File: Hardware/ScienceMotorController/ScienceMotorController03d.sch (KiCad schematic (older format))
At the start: 16 parts

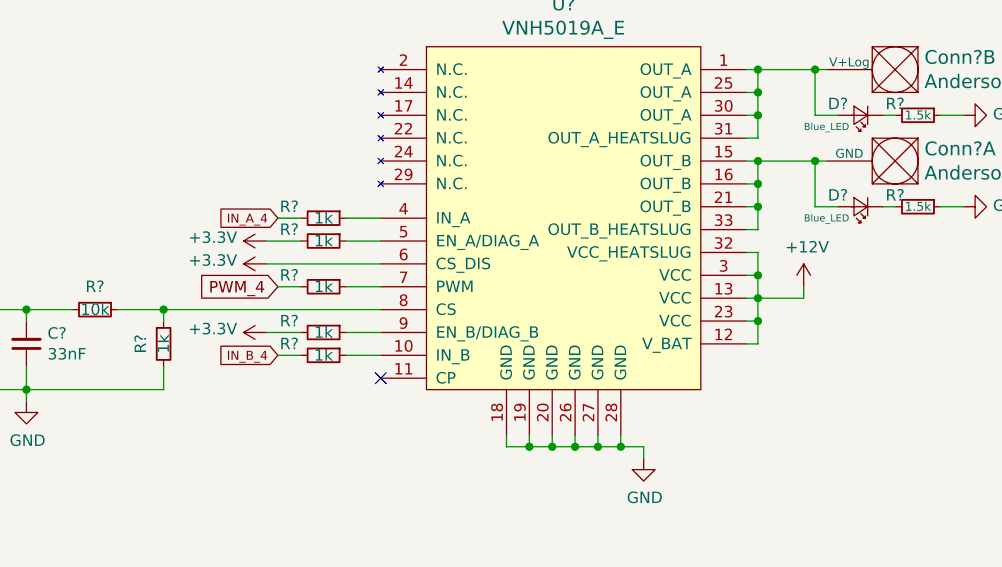
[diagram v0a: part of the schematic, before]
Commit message: changed everything to actuation, added schottky diode, added A/B flags to tiva
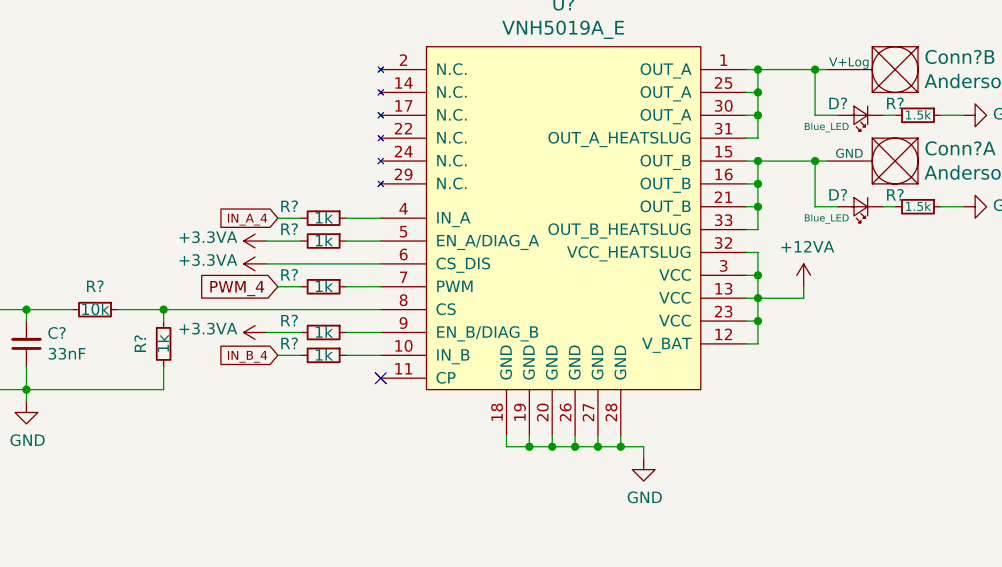
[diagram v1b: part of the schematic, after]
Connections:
- net +12V renamed +12VA
- net +3V3 renamed +3.3VA
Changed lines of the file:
@@
 	6800 4300 6800 4200
 Connection ~ 6800 4200
-$Comp
-L power:+12V #PWR?
-U 1 1 5FA97817
-P 7000 4050
-AR Path="/5F7D111E/5FA97817" Ref="#PWR?"  Part="1"
-AR Path="/5F7D111E/5FA6640B/5FA97817" Ref="#PWR?"  Part="1"
-F 0 "#PWR?" H 7000 3900 50  0001 C CNN
-F 1 "+12V" H 7015 4223 50  0000 C CNN
-F 2 "" H 7000 4050 50  0001 C CNN
-F 3 "" H 7000 4050 50  0001 C CNN
-	1    7000 4050
-	1    0    0    -1
-$EndComp
 Wire Wire Line
 	7000 4050 7000 4100
@@
 Wire Wire Line
 	4800 4250 4650 4250
-$Comp
-L power:+3.3V #PWR?
-U 1 1 5FA97858
-P 4650 4250
-AR Path="/5F7D111E/5FA97858" Ref="#PWR?"  Part="1"
-AR Path="/5F7D111E/5FA6640B/5FA97858" Ref="#PWR?"  Part="1"
-F 0 "#PWR?" H 4650 4100 50  0001 C CNN
-F 1 "+3.3V" V 4665 4378 50  0000 L CNN
-F 2 "" H 4650 4250 50  0001 C CNN
-F 3 "" H 4650 4250 50  0001 C CNN
-	1    4650 4250
-	0    -1   -1   0
-$EndComp
-$Comp
-L power:+3.3V #PWR?
-U 1 1 5FA9785E
-P 4650 3950
-AR Path="/5F7D111E/5FA9785E" Ref="#PWR?"  Part="1"
-AR Path="/5F7D111E/5FA6640B/5FA9785E" Ref="#PWR?"  Part="1"
-F 0 "#PWR?" H 4650 3800 50  0001 C CNN
-F 1 "+3.3V" V 4665 4078 50  0000 L CNN
-F 2 "" H 4650 3950 50  0001 C CNN
-F 3 "" H 4650 3950 50  0001 C CNN
-	1    4650 3950
-	0    -1   -1   0
-$EndComp
 Wire Wire Line
 	5150 3950 4650 3950
@@
 Wire Wire Line
 	5150 3850 5000 3850
-$Comp
-L power:+3.3V #PWR?
-U 1 1 5FA9786C
-P 4650 3850
-AR Path="/5F7D111E/5FA9786C" Ref="#PWR?"  Part="1"
-AR Path="/5F7D111E/5FA6640B/5FA9786C" Ref="#PWR?"  Part="1"
-F 0 "#PWR?" H 4650 3700 50  0001 C CNN
-F 1 "+3.3V" V 4665 3978 50  0000 L CNN
-F 2 "" H 4650 3850 50  0001 C CNN
-F 3 "" H 4650 3850 50  0001 C CNN
-	1    4650 3850
-	0    -1   -1   0
-$EndComp
 Wire Wire Line
 	4800 3850 4650 3850
@@
 Text Notes 7150 6900 0    197  ~ 0
 Sheet 03d: Motor Driver 4
+$Comp
+L power:+12VA #PWR?
+U 1 1 5F837D8D
+P 7000 4050
+F 0 "#PWR?" H 7000 3900 50  0001 C CNN
+F 1 "+12VA" H 7015 4223 50  0000 C CNN
+F 2 "" H 7000 4050 50  0001 C CNN
+F 3 "" H 7000 4050 50  0001 C CNN
+	1    7000 4050
+	1    0    0    -1
+$EndComp
+$Comp
+L power:+3.3VA #PWR?
+U 1 1 5F838A13
+P 4650 3850
+F 0 "#PWR?" H 4650 3700 50  0001 C CNN
+F 1 "+3.3VA" V 4665 3977 50  0000 L CNN
+F 2 "" H 4650 3850 50  0001 C CNN
+F 3 "" H 4650 3850 50  0001 C CNN
+	1    4650 3850
+	0    -1   -1   0
+$EndComp
+$Comp
+L power:+3.3VA #PWR?
+U 1 1 5F83A598
+P 4650 3950
+F 0 "#PWR?" H 4650 3800 50  0001 C CNN
+F 1 "+3.3VA" V 4665 4077 50  0000 L CNN
+F 2 "" H 4650 3950 50  0001 C CNN
+F 3 "" H 4650 3950 50  0001 C CNN
+	1    4650 3950
+	0    -1   -1   0
+$EndComp
+$Comp
+L power:+3.3VA #PWR?
+U 1 1 5F83A969
+P 4650 4250
+F 0 "#PWR?" H 4650 4100 50  0001 C CNN
+F 1 "+3.3VA" V 4665 4377 50  0000 L CNN
+F 2 "" H 4650 4250 50  0001 C CNN
+F 3 "" H 4650 4250 50  0001 C CNN
+	1    4650 4250
+	0    -1   -1   0
+$EndComp
 $EndSCHEMATC

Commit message: fixed hierarchical
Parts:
- added FB? (x2): Ferrite_Bead, symbol Device:Ferrite_Bead_Small
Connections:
- net at U?.1 (OUT_A), U?.25 (OUT_A), U?.30 (OUT_A)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: now also FB?.2; no longer Conn?.2 (V+Log), D?.2 (A)
- net at U?.15 (OUT_B), U?.16 (OUT_B), U?.21 (OUT_B)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: now also FB?.2; no longer Conn?.1 (GND), D?.2 (A)
- net IN_A_4 renamed In_A_4
- net IN_B_4 renamed In_B_4
- new net: Conn?.2 (V+Log), D?.2 (A), FB?.1
- new net: Conn?.1 (GND), D?.2 (A), FB?.1
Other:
- moved on the sheet: Conn?A, Conn?B, D?, R?

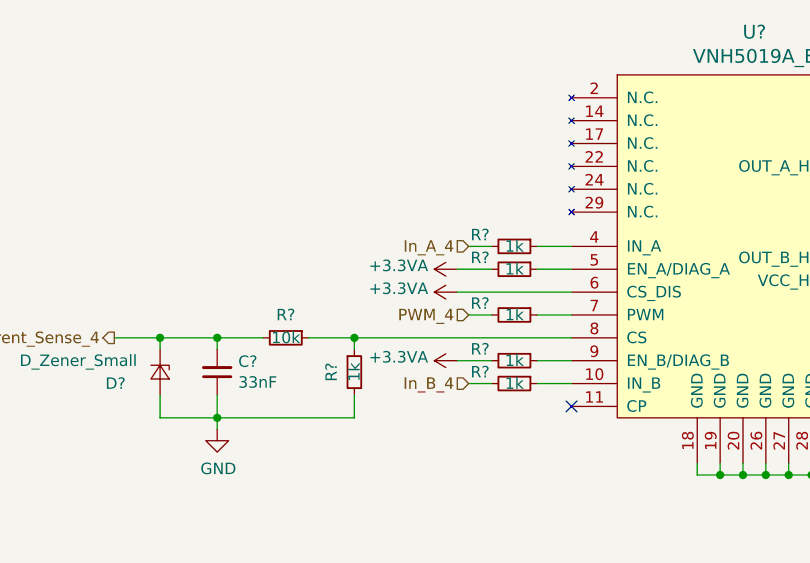
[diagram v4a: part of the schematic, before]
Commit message: Fixed 3.3V, added encoders
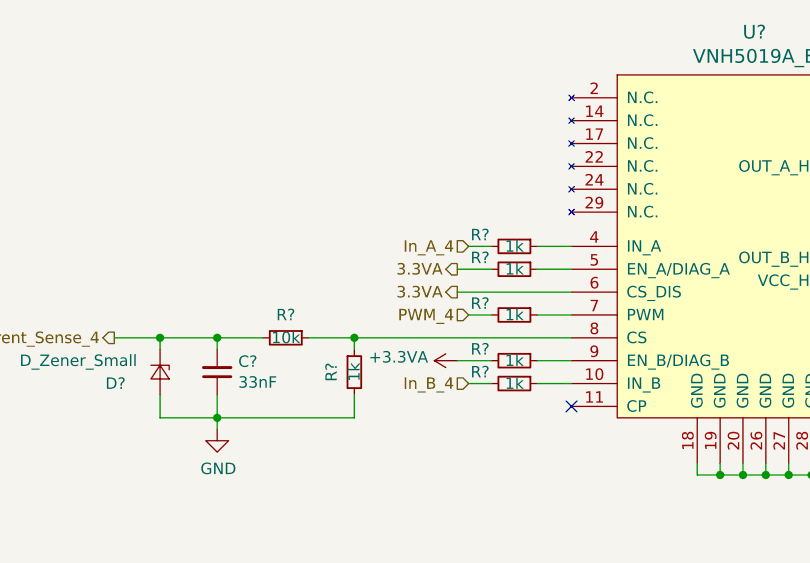
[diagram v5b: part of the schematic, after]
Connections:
- net +3.3VA: no longer R?.2, U?.6 (CS_DIS)
- new net 3.3VA: R?.2, U?.6 (CS_DIS)
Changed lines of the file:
@@
 $Descr A4 11693 8268
 encoding utf-8
-Sheet 6 10
+Sheet 6 11
 Title ""
 Date ""
@@
 $Comp
 L power:+3.3VA #PWR?
-U 1 1 5F83A598
-P 4650 3950
-AR Path="/5F7D111E/5FA6640B/5F83A598" Ref="#PWR?"  Part="1"
-AR Path="/5F9082FC/5F83A598" Ref="#PWR?"  Part="1"
-AR Path="/5F7148FA/5FA34AD9/5F83A598" Ref="#PWR?"  Part="1"
-F 0 "#PWR?" H 4650 3800 50  0001 C CNN
-F 1 "+3.3VA" V 4665 4077 50  0000 L CNN
-F 2 "" H 4650 3950 50  0001 C CNN
-F 3 "" H 4650 3950 50  0001 C CNN
-	1    4650 3950
-	0    -1   -1   0
-$EndComp
-$Comp
-L power:+3.3VA #PWR?
 U 1 1 5F83A969
 P 4650 4250
@@
 Text HLabel 4700 3750 0    50   Input ~ 0
 In_A_4
-$Comp
-L power:+3.3VA #PWR?
-U 1 1 5F838A13
-P 4650 3850
-AR Path="/5F7D111E/5FA6640B/5F838A13" Ref="#PWR?"  Part="1"
-AR Path="/5F9082FC/5F838A13" Ref="#PWR?"  Part="1"
-AR Path="/5F7148FA/5FA34AD9/5F838A13" Ref="#PWR?"  Part="1"
-F 0 "#PWR?" H 4650 3700 50  0001 C CNN
-F 1 "+3.3VA" V 4665 3977 50  0000 L CNN
-F 2 "" H 4650 3850 50  0001 C CNN
-F 3 "" H 4650 3850 50  0001 C CNN
-	1    4650 3850
-	0    -1   -1   0
-$EndComp
 Text HLabel 4700 4350 0    50   Input ~ 0
 In_B_4
@@
 Text HLabel 3150 4150 0    50   Output ~ 0
 Current_Sense_4
+Text HLabel 4650 3850 0    50   Output ~ 0
+3.3VA
+Text HLabel 4650 3950 0    50   Output ~ 0
+3.3VA
 $EndSCHEMATC

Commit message: added logic line
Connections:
- net 3.3VA is gone; now on net 3.3V: R?.2, U?.6 (CS_DIS)
- net +3.3VA renamed 3.3V
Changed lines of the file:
@@
-$EndComp
-$Comp
-L power:+3.3VA #PWR?
-U 1 1 5F83A969
-P 4650 4250
-AR Path="/5F7D111E/5FA6640B/5F83A969" Ref="#PWR?"  Part="1"
-AR Path="/5F9082FC/5F83A969" Ref="#PWR?"  Part="1"
-AR Path="/5F7148FA/5FA34AD9/5F83A969" Ref="#PWR?"  Part="1"
-F 0 "#PWR?" H 4650 4100 50  0001 C CNN
-F 1 "+3.3VA" V 4665 4377 50  0000 L CNN
-F 2 "" H 4650 4250 50  0001 C CNN
-F 3 "" H 4650 4250 50  0001 C CNN
-	1    4650 4250
-	0    -1   -1   0
 $EndComp
 $Comp
@@
 Current_Sense_4
 Text HLabel 4650 3850 0    50   Output ~ 0
-3.3VA
+3.3V
 Text HLabel 4650 3950 0    50   Output ~ 0
-3.3VA
+3.3V
+Text HLabel 4650 4250 0    50   Output ~ 0
+3.3V
 $EndSCHEMATC

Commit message: annotated
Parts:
- C5: renamed from C?; footprint (none) -> Capacitor_SMD:C_0603_1608Metric_Pad1.05x0.95mm_HandSolder
- gave numbers to parts that had none: 16
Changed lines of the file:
@@
 AR Path="/5F7D111E/5FA6640B/5FA97805" Ref="U?"  Part="1"
 AR Path="/5F9082FC/5FA97805" Ref="U?"  Part="1"
-AR Path="/5F7148FA/5FA34AD9/5FA97805" Ref="U?"  Part="1"
-F 0 "U?" H 5950 6187 60  0000 C CNN
+AR Path="/5F7148FA/5FA34AD9/5FA97805" Ref="U5"  Part="1"
+F 0 "U5" H 5950 6187 60  0000 C CNN
 F 1 "VNH5019A_E" H 5950 6081 60  0000 C CNN
 F 2 "" H 5350 5800 60  0001 C CNN
@@
 AR Path="/5F7D111E/5FA6640B/5FA97822" Ref="R?"  Part="1"
 AR Path="/5F9082FC/5FA97822" Ref="R?"  Part="1"
-AR Path="/5F7148FA/5FA34AD9/5FA97822" Ref="R?"  Part="1"
-F 0 "R?" V 4850 3900 50  0000 C CNN
+AR Path="/5F7148FA/5FA34AD9/5FA97822" Ref="R28"  Part="1"
+F 0 "R28" V 4850 3900 50  0000 C CNN
 F 1 "1k" V 4900 4050 50  0000 C CNN
 F 2 "" H 4900 4050 50  0001 C CNN
@@
 AR Path="/5F7D111E/5FA6640B/5FA97828" Ref="R?"  Part="1"
 AR Path="/5F9082FC/5FA97828" Ref="R?"  Part="1"
-AR Path="/5F7148FA/5FA34AD9/5FA97828" Ref="R?"  Part="1"
-F 0 "R?" V 4100 4300 50  0000 C CNN
+AR Path="/5F7148FA/5FA34AD9/5FA97828" Ref="R25"  Part="1"
+F 0 "R25" V 4100 4300 50  0000 C CNN
 F 1 "1k" V 4200 4300 50  0000 C CNN
 F 2 "" H 4200 4300 50  0001 C CNN
@@
 AR Path="/5F7D111E/5FA6640B/5FA9782E" Ref="C?"  Part="1"
 AR Path="/5F9082FC/5FA9782E" Ref="C?"  Part="1"
-AR Path="/5F7148FA/5FA34AD9/5FA9782E" Ref="C?"  Part="1"
-F 0 "C?" H 3508 4254 50  0000 R CNN
+AR Path="/5F7148FA/5FA34AD9/5FA9782E" Ref="C5"  Part="1"
+F 0 "C5" H 3508 4254 50  0000 R CNN
 F 1 "33nF" H 3508 4345 50  0000 R CNN
-F 2 "" H 3600 4300 50  0001 C CNN
+F 2 "Capacitor_SMD:C_0603_1608Metric_Pad1.05x0.95mm_HandSolder" H 3600 4300 50  0001 C CNN
 F 3 "~" H 3600 4300 50  0001 C CNN
 	1    3600 4300
@@
 AR Path="/5F7D111E/5FA6640B/5FA97834" Ref="D?"  Part="1"
 AR Path="/5F9082FC/5FA97834" Ref="D?"  Part="1"
-AR Path="/5F7148FA/5FA34AD9/5FA97834" Ref="D?"  Part="1"
-F 0 "D?" V 3400 4150 50  0000 R CNN
+AR Path="/5F7148FA/5FA34AD9/5FA97834" Ref="D13"  Part="1"
+F 0 "D13" V 3400 4150 50  0000 R CNN
 F 1 "D_Zener_Small" V 3300 4200 50  0000 R CNN
 F 2 "" V 3350 4300 50  0001 C CNN
@@
 AR Path="/5F7D111E/5FA6640B/5FA9783A" Ref="R?"  Part="1"
 AR Path="/5F9082FC/5FA9783A" Ref="R?"  Part="1"
-AR Path="/5F7148FA/5FA34AD9/5FA9783A" Ref="R?"  Part="1"
-F 0 "R?" V 3800 4150 50  0000 C CNN
+AR Path="/5F7148FA/5FA34AD9/5FA9783A" Ref="R24"  Part="1"
+F 0 "R24" V 3800 4150 50  0000 C CNN
 F 1 "10k" V 3900 4150 50  0000 C CNN
 F 2 "" H 3900 4150 50  0001 C CNN
@@
 AR Path="/5F7D111E/5FA6640B/5FA97850" Ref="R?"  Part="1"
 AR Path="/5F9082FC/5FA97850" Ref="R?"  Part="1"
-AR Path="/5F7148FA/5FA34AD9/5FA97850" Ref="R?"  Part="1"
-F 0 "R?" V 4850 4100 50  0000 C CNN
+AR Path="/5F7148FA/5FA34AD9/5FA97850" Ref="R29"  Part="1"
+F 0 "R29" V 4850 4100 50  0000 C CNN
 F 1 "1k" V 4900 4250 50  0000 C CNN
 F 2 "" H 4900 4250 50  0001 C CNN
@@
 AR Path="/5F7D111E/5FA6640B/5FA97865" Ref="R?"  Part="1"
 AR Path="/5F9082FC/5FA97865" Ref="R?"  Part="1"
-AR Path="/5F7148FA/5FA34AD9/5FA97865" Ref="R?"  Part="1"
-F 0 "R?" V 4850 3700 50  0000 C CNN
+AR Path="/5F7148FA/5FA34AD9/5FA97865" Ref="R27"  Part="1"
+F 0 "R27" V 4850 3700 50  0000 C CNN
 F 1 "1k" V 4900 3850 50  0000 C CNN
 F 2 "" H 4900 3850 50  0001 C CNN
@@
 AR Path="/5F7D111E/5FA6640B/5FA97873" Ref="R?"  Part="1"
 AR Path="/5F9082FC/5FA97873" Ref="R?"  Part="1"
-AR Path="/5F7148FA/5FA34AD9/5FA97873" Ref="R?"  Part="1"
-F 0 "R?" V 4850 3600 50  0000 C CNN
+AR Path="/5F7148FA/5FA34AD9/5FA97873" Ref="R26"  Part="1"
+F 0 "R26" V 4850 3600 50  0000 C CNN
 F 1 "1k" V 4900 3750 50  0000 C CNN
 F 2 "" H 4900 3750 50  0001 C CNN
@@
 AR Path="/5F7D111E/5FA6640B/5FA9787D" Ref="R?"  Part="1"
 AR Path="/5F9082FC/5FA9787D" Ref="R?"  Part="1"
-AR Path="/5F7148FA/5FA34AD9/5FA9787D" Ref="R?"  Part="1"
-F 0 "R?" V 4850 4200 50  0000 C CNN
+AR Path="/5F7148FA/5FA34AD9/5FA9787D" Ref="R30"  Part="1"
+F 0 "R30" V 4850 4200 50  0000 C CNN
 F 1 "1k" V 4900 4350 50  0000 C CNN
 F 2 "" H 4900 4350 50  0001 C CNN
@@
 AR Path="/5F7D111E/5FA6640B/5FA97895" Ref="#PWR?"  Part="1"
 AR Path="/5F9082FC/5FA97895" Ref="#PWR?"  Part="1"
-AR Path="/5F7148FA/5FA34AD9/5FA97895" Ref="#PWR?"  Part="1"
-F 0 "#PWR?" H 6300 4550 50  0001 C CNN
+AR Path="/5F7148FA/5FA34AD9/5FA97895" Ref="#PWR027"  Part="1"
+F 0 "#PWR027" H 6300 4550 50  0001 C CNN
 F 1 "GND" H 6305 4627 50  0000 C CNN
 F 2 "" H 6300 4800 50  0001 C CNN
@@
 AR Path="/5F7D111E/5FA6640B/5FA9789F" Ref="#PWR?"  Part="1"
 AR Path="/5F9082FC/5FA9789F" Ref="#PWR?"  Part="1"
-AR Path="/5F7148FA/5FA34AD9/5FA9789F" Ref="#PWR?"  Part="1"
-F 0 "#PWR?" H 3600 4300 50  0001 C CNN
+AR Path="/5F7148FA/5FA34AD9/5FA9789F" Ref="#PWR026"  Part="1"
+F 0 "#PWR026" H 3600 4300 50  0001 C CNN
 F 1 "GND" H 3605 4377 50  0000 C CNN
 F 2 "" H 3600 4550 50  0001 C CNN
@@
 AR Path="/5F7D111E/5FA6640B/5FA978B7" Ref="Conn?"  Part="1"
 AR Path="/5F9082FC/5FA978B7" Ref="Conn?"  Part="1"
-AR Path="/5F7148FA/5FA34AD9/5FA978B7" Ref="Conn?"  Part="1"
-F 0 "Conn?" H 7922 3447 60  0000 R CNN
+AR Path="/5F7148FA/5FA34AD9/5FA978B7" Ref="Conn4"  Part="1"
+F 0 "Conn4" H 7922 3447 60  0000 R CNN
 F 1 "AndersonPP" H 7922 3553 60  0000 R CNN
 F 2 "" H 7800 2850 60  0001 C CNN
@@
 AR Path="/5F7D111E/5FA6640B/5FA978BD" Ref="Conn?"  Part="2"
 AR Path="/5F9082FC/5FA978BD" Ref="Conn?"  Part="2"
-AR Path="/5F7148FA/5FA34AD9/5FA978BD" Ref="Conn?"  Part="2"
-F 0 "Conn?" H 7922 3047 60  0000 R CNN
+AR Path="/5F7148FA/5FA34AD9/5FA978BD" Ref="Conn4"  Part="2"
+F 0 "Conn4" H 7922 3047 60  0000 R CNN
 F 1 "AndersonPP" H 7922 3153 60  0000 R CNN
 F 2 "" H 7800 2450 60  0001 C CNN
@@
 AR Path="/5F7D111E/5FA6640B/5FA978D1" Ref="D?"  Part="1"
 AR Path="/5F9082FC/5FA978D1" Ref="D?"  Part="1"
-AR Path="/5F7148FA/5FA34AD9/5FA978D1" Ref="D?"  Part="1"
-F 0 "D?" H 7800 3250 50  0000 C CNN
+AR Path="/5F7148FA/5FA34AD9/5FA978D1" Ref="D14"  Part="1"
+F 0 "D14" H 7800 3250 50  0000 C CNN
 F 1 "Blue_LED" H 7850 3350 31  0000 C CNN
 F 2 "" V 7700 3300 50  0001 C CNN
@@
 AR Path="/5F7D111E/5FA6640B/5FA978D7" Ref="D?"  Part="1"
 AR Path="/5F9082FC/5FA978D7" Ref="D?"  Part="1"
-AR Path="/5F7148FA/5FA34AD9/5FA978D7" Ref="D?"  Part="1"
-F 0 "D?" H 7800 3650 50  0000 C CNN
+AR Path="/5F7148FA/5FA34AD9/5FA978D7" Ref="D15"  Part="1"
+F 0 "D15" H 7800 3650 50  0000 C CNN
 F 1 "Blue_LED" H 7850 3750 31  0000 C CNN
 F 2 "" V 7700 3700 50  0001 C CNN
@@
 AR Path="/5F7D111E/5FA6640B/5FA978DD" Ref="R?"  Part="1"
 AR Path="/5F9082FC/5FA978DD" Ref="R?"  Part="1"
-AR Path="/5F7148FA/5FA34AD9/5FA978DD" Ref="R?"  Part="1"
-F 0 "R?" V 7900 3600 50  0000 C CNN
+AR Path="/5F7148FA/5FA34AD9/5FA978DD" Ref="R32"  Part="1"
+F 0 "R32" V 7900 3600 50  0000 C CNN
 F 1 "1.5k" V 7950 3700 39  0000 C CNN
 F 2 "" H 7950 3700 50  0001 C CNN
@@
 AR Path="/5F7D111E/5FA6640B/5FA978E3" Ref="R?"  Part="1"
 AR Path="/5F9082FC/5FA978E3" Ref="R?"  Part="1"
-AR Path="/5F7148FA/5FA34AD9/5FA978E3" Ref="R?"  Part="1"
-F 0 "R?" V 7900 3200 50  0000 C CNN
+AR Path="/5F7148FA/5FA34AD9/5FA978E3" Ref="R31"  Part="1"
+F 0 "R31" V 7900 3200 50  0000 C CNN
 F 1 "1.5k" V 7950 3300 39  0000 C CNN
 F 2 "" H 7950 3300 50  0001 C CNN
@@
 AR Path="/5F7D111E/5FA6640B/5FA978EB" Ref="#PWR?"  Part="1"
 AR Path="/5F9082FC/5FA978EB" Ref="#PWR?"  Part="1"
-AR Path="/5F7148FA/5FA34AD9/5FA978EB" Ref="#PWR?"  Part="1"
-F 0 "#PWR?" H 8150 3050 50  0001 C CNN
+AR Path="/5F7148FA/5FA34AD9/5FA978EB" Ref="#PWR029"  Part="1"
+F 0 "#PWR029" H 8150 3050 50  0001 C CNN
 F 1 "GND" V 8155 3172 50  0000 R CNN
 F 2 "" H 8150 3300 50  0001 C CNN
@@
 AR Path="/5F7D111E/5FA6640B/5FA978F1" Ref="#PWR?"  Part="1"
 AR Path="/5F9082FC/5FA978F1" Ref="#PWR?"  Part="1"
-AR Path="/5F7148FA/5FA34AD9/5FA978F1" Ref="#PWR?"  Part="1"
-F 0 "#PWR?" H 8150 3450 50  0001 C CNN
+AR Path="/5F7148FA/5FA34AD9/5FA978F1" Ref="#PWR030"  Part="1"
+F 0 "#PWR030" H 8150 3450 50  0001 C CNN
 F 1 "GND" V 8155 3572 50  0000 R CNN
 F 2 "" H 8150 3700 50  0001 C CNN
@@
 AR Path="/5F7D111E/5FA6640B/5F837D8D" Ref="#PWR?"  Part="1"
 AR Path="/5F9082FC/5F837D8D" Ref="#PWR?"  Part="1"
-AR Path="/5F7148FA/5FA34AD9/5F837D8D" Ref="#PWR?"  Part="1"
-F 0 "#PWR?" H 7000 3900 50  0001 C CNN
+AR Path="/5F7148FA/5FA34AD9/5F837D8D" Ref="#PWR028"  Part="1"
+F 0 "#PWR028" H 7000 3900 50  0001 C CNN
 F 1 "+12VA" H 7015 4223 50  0000 C CNN
 F 2 "" H 7000 4050 50  0001 C CNN
@@
 P 7150 3100
 AR Path="/5F9082FC/5F9ECC76" Ref="FB?"  Part="1"
-AR Path="/5F7148FA/5FA34AD9/5F9ECC76" Ref="FB?"  Part="1"
-F 0 "FB?" V 6913 3100 50  0000 C CNN
+AR Path="/5F7148FA/5FA34AD9/5F9ECC76" Ref="FB5"  Part="1"
+F 0 "FB5" V 6913 3100 50  0000 C CNN
 F 1 "Ferrite_Bead" V 7004 3100 50  0000 C CNN
 F 2 "" V 7080 3100 50  0001 C CNN
@@
 P 7150 3500
 AR Path="/5F9082FC/5F9ED41C" Ref="FB?"  Part="1"
-AR Path="/5F7148FA/5FA34AD9/5F9ED41C" Ref="FB?"  Part="1"
-F 0 "FB?" V 6913 3500 50  0000 C CNN
+AR Path="/5F7148FA/5FA34AD9/5F9ED41C" Ref="FB6"  Part="1"
+F 0 "FB6" V 6913 3500 50  0000 C CNN
 F 1 "Ferrite_Bead" V 7004 3500 50  0000 C CNN
 F 2 "" V 7080 3500 50  0001 C CNN
